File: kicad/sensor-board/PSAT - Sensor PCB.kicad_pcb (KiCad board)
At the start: 2 copper layers, 54.5 x 54.5 mm, 44 parts, among them J1 533980471, J2 533980471, J3 533980471, J4 533980471, Q1 2N2222A, U1 ESP32-CAM, U2 CD-PA1616D, U3 BME280, U4 BMI323

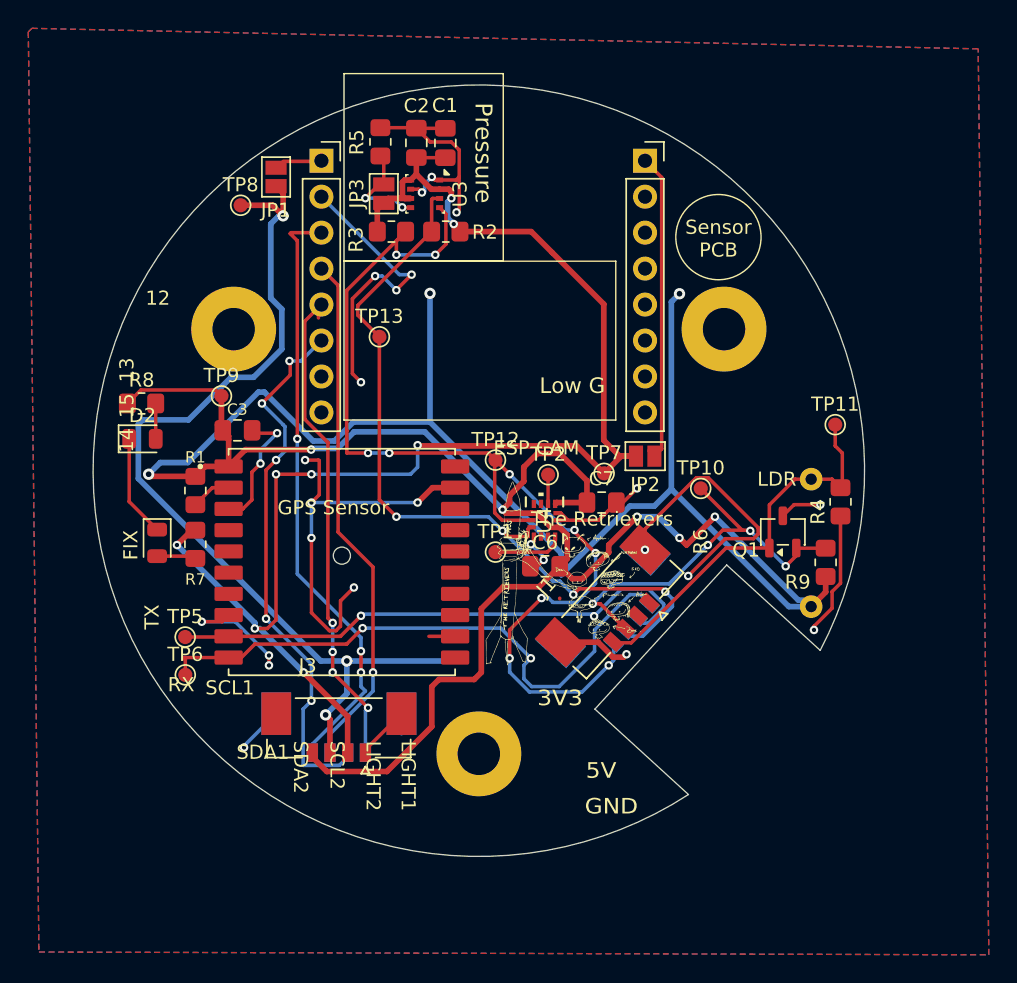
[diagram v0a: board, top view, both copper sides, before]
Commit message: feat: sensor board pcb wiring, silkscreen incomplete
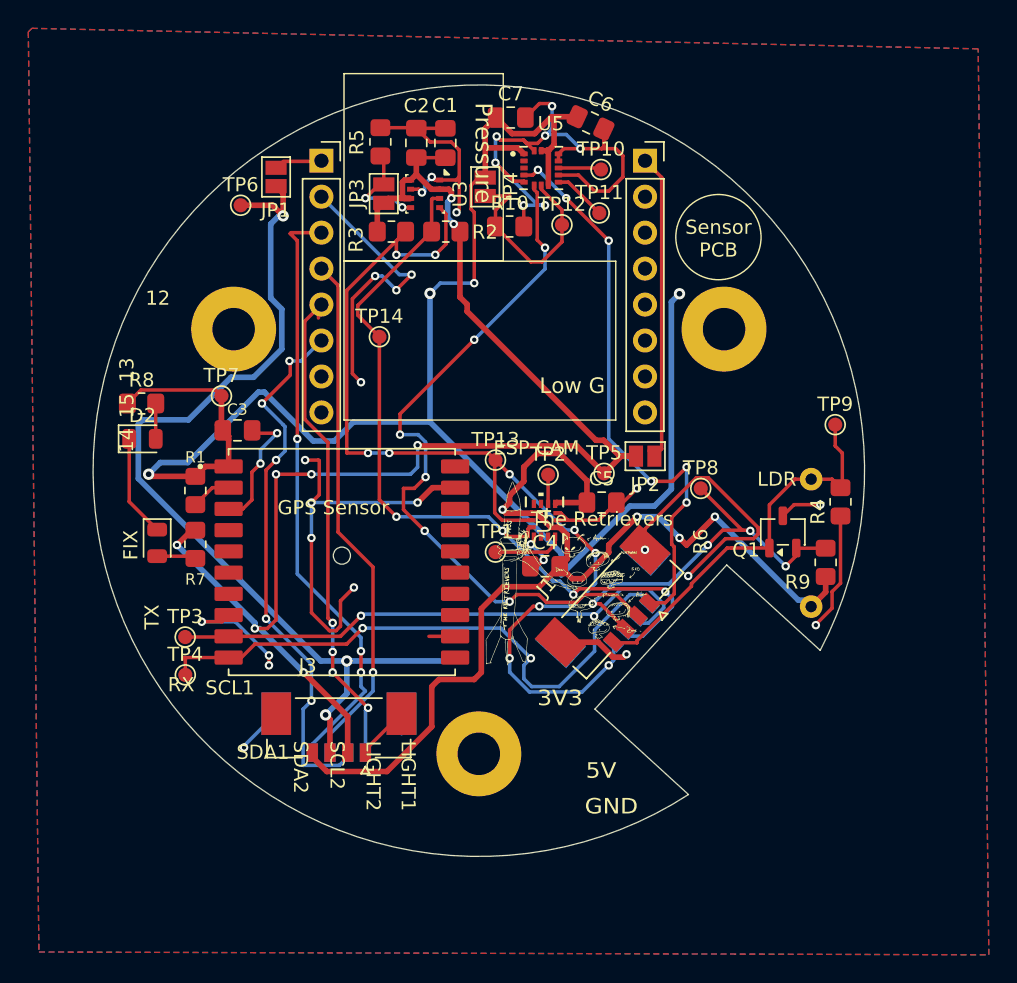
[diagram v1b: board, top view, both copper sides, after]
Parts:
- added C6: 10uF, Capacitor_SMD:C_0805_2012Metric_Pad1.18x1.45mm_HandSolder, F.Cu at (150.2, 72.7)
- added C7: 100nF, Capacitor_SMD:C_0805_2012Metric_Pad1.18x1.45mm_HandSolder, F.Cu at (144.6, 72.3)
- added JP4: EN_5, Jumper:SolderJumper-2_P1.3mm_Open_Pad1.0x1.5mm, F.Cu at (142.8, 77.2)
- added R10: 1Meg, Resistor_SMD:R_0805_2012Metric_Pad1.20x1.40mm_HandSolder, F.Cu at (144.5, 80.0)
- added TP10: TestPoint, TestPoint:TestPoint_Pad_D1.0mm, F.Cu at (151.0, 76.0)
- added TP11: TestPoint, TestPoint:TestPoint_Pad_D1.0mm, F.Cu at (150.8, 79.0)
- added TP12: TestPoint, TestPoint:TestPoint_Pad_D1.0mm, F.Cu at (148.2, 79.9)
- added U5: H3LIS100DLTR, PSAT_Library:PQFN50P300X300X100-16N, F.Cu at (146.7, 75.9)
- renumbered C6 to C4, C7 to C5, TP12 to TP13, TP13 to TP14, TP5 to TP3, TP6 to TP4, TP7 to TP5, TP8 to TP6, TP9 to TP7, TP10 to TP8, TP11 to TP9, U2 to U1, U1 to U2
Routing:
- net SDA2: track 0.02 -> 50.6 mm, vias 0 -> 6
- net SCL2: track 0.00 -> 40.9 mm, vias 0 -> 6
- net GND: track 148.7 -> 186.9 mm, vias 26 -> 33
- net SA0: track 0.00 -> 15.2 mm
- net 3V3_LDO: track 203.2 -> 199.1 mm
- net IN2_100: track 0.00 -> 3.78 mm
- net INT1_100: track 0.00 -> 3.05 mm
- net 3V3_BUCK: track 103.8 -> 101.2 mm

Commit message: feat: Wiring PCB adding silkscreen
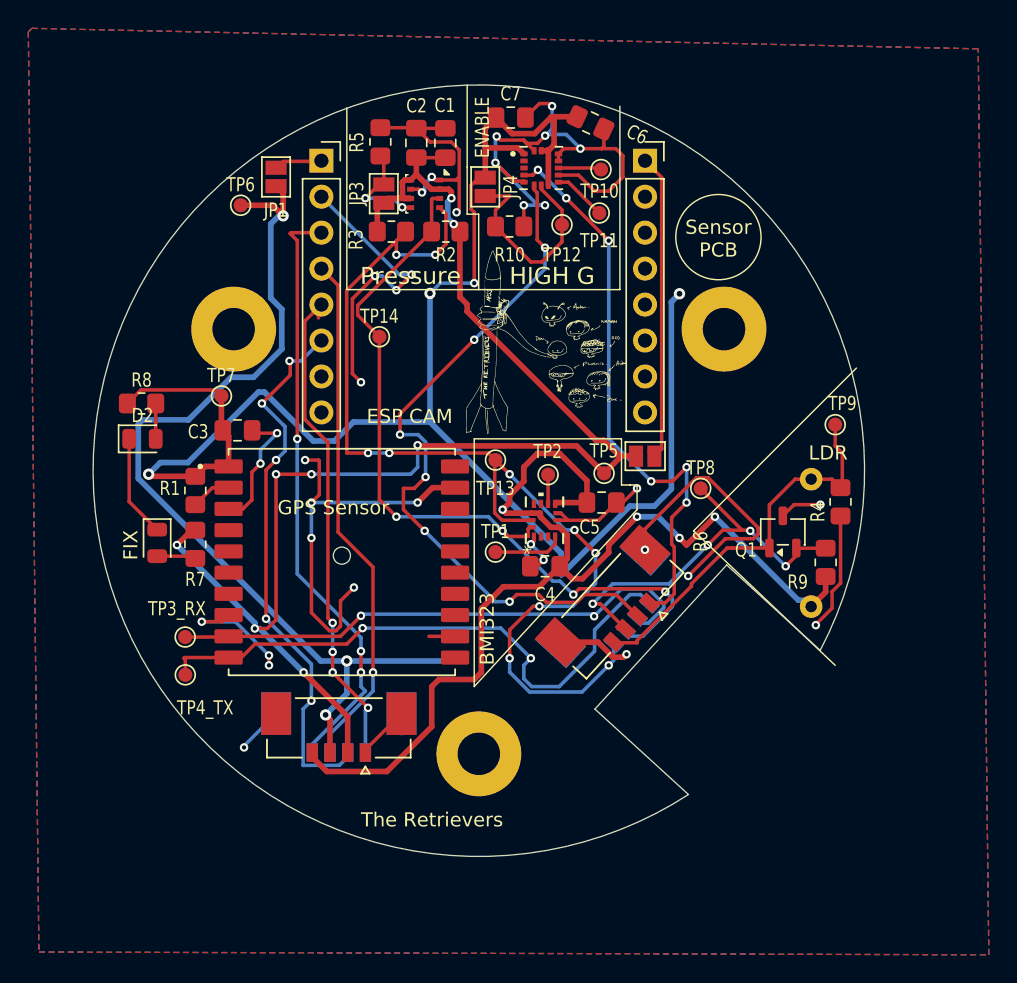
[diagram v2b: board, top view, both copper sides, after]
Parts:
- moved G*** 16.4 mm to (147.1, 89.5)
- renumbered U3 to ENABLE, U5 to ESP32, TP3 to TP3_RX, TP4 to TP4_TX
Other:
- board text added: "BMI323"
- board text added: "HIGH G"
- board text removed: "12"
- board text removed: "13"
- board text removed: "14"
- board text removed: "15"
- board text removed: "3V3"
- board text removed: "5V"
- board text removed: "GND"
- board text removed: "LIGHT1"
- board text removed: "LIGHT2"
- board text removed: "Low G"
- board text removed: "RX"
- board text removed: "SCL1"
- board text removed: "SCL2"
- board text removed: "SDA1"
- board text removed: "SDA2"
- board text removed: "TX"
